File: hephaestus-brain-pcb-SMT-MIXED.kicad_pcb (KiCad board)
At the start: 2 copper layers, 26 x 49 mm, 31 parts, among them IC1 ATSAMD51G19A-MU, J1 Barrel_Jack, J2 Conn_02x03_Odd_Even, J3 USB_B_Micro, J5 Conn_01x03_Male, J6 Conn_01x03_Male, J7 Conn_01x03_Male, SW1 SW_SPDT, SW2 SW_SPST, SW3 SW_SPST, U1 LM1117-5.0, U2 AP2112K-3.3, U3 AT25xxx-MA, U4 74LVC1G125

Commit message: routing tweaks
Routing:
- net +5V: track 33.1 -> 33.7 mm
- net RX: vias 1 -> 2

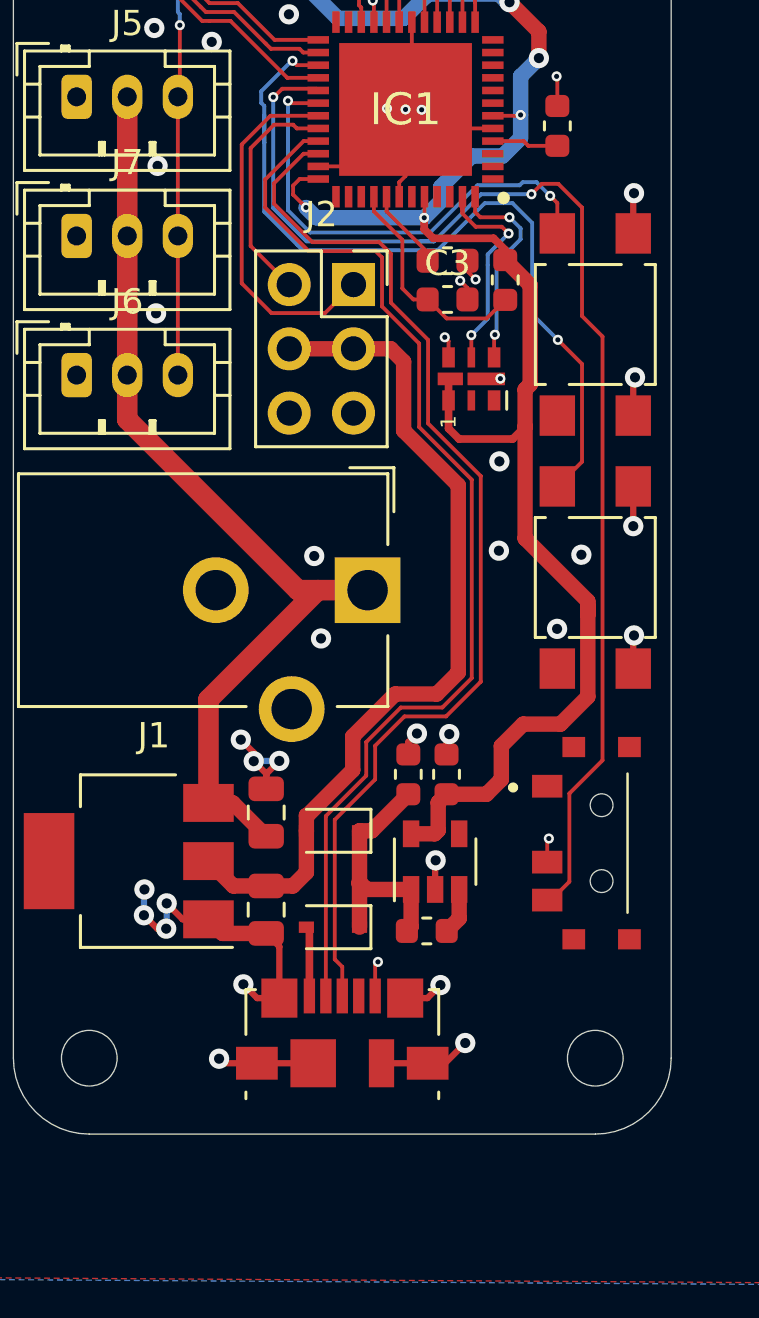
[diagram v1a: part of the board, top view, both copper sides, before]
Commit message: Switched over to USBC connector.
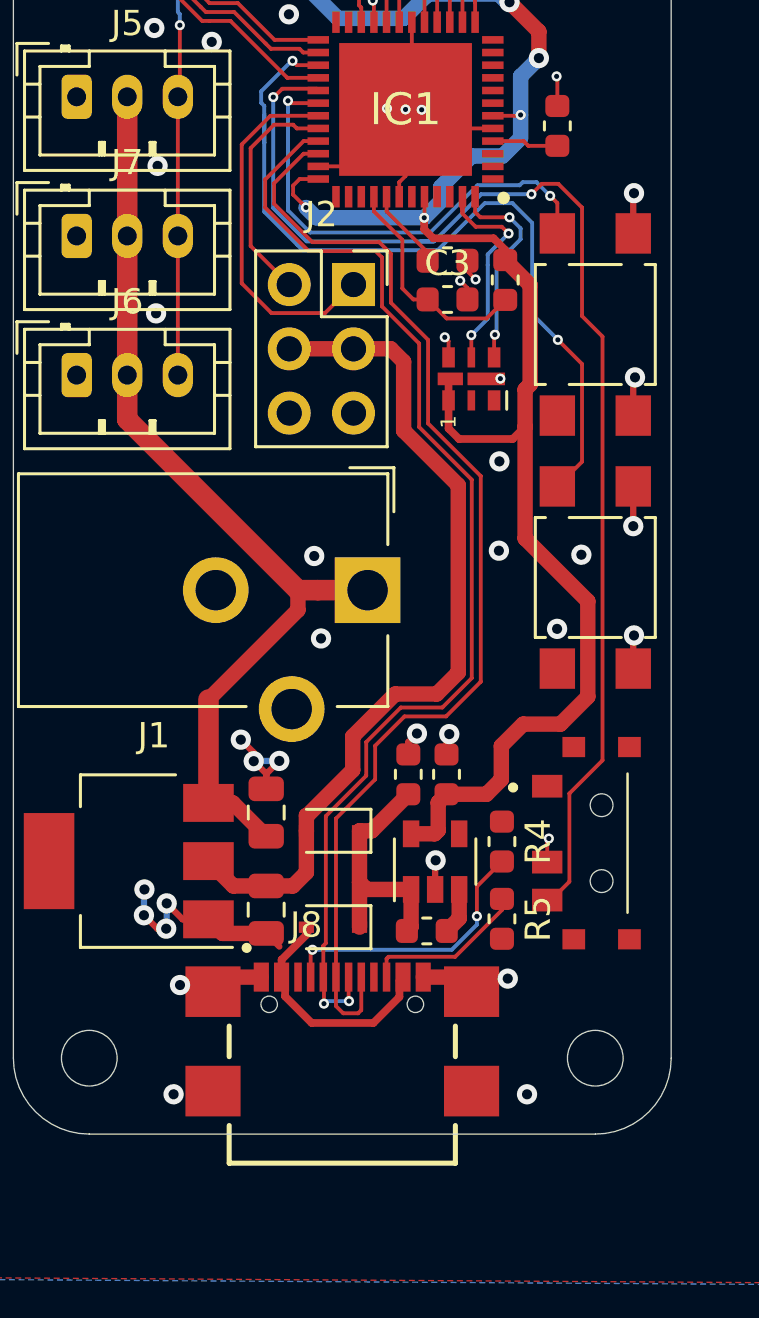
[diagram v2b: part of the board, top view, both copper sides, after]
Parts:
- removed J3: USB_B_Micro, Connector_USB:USB_Micro-B_Molex_47346-0001
- added J8: USB4110-GF-A, unified:GCT_USB4110-GF-A, F.Cu at (123.0, 102.9)
- added R4: 5.1k, Resistor_SMD:R_0603_1608Metric, F.Cu at (129.3, 96.4)
- added R5: 5.1k, Resistor_SMD:R_0603_1608Metric, F.Cu at (129.3, 99.5)
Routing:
- net Net-(J8-PadA5): track 0.00 -> 10.9 mm, vias 0 -> 2
- net GND: track 77.1 -> 67.2 mm, vias 42 -> 41
- net +5VP: track 2.77 -> 9.59 mm
- net Net-(J8-PadB5): track 0.00 -> 6.52 mm
- net D+: track 42.8 -> 45.5 mm
- net D-: track 43.3 -> 45.6 mm, vias 0 -> 2
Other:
- rule pad_to_mask_clearance: 0.051 -> 0.0005

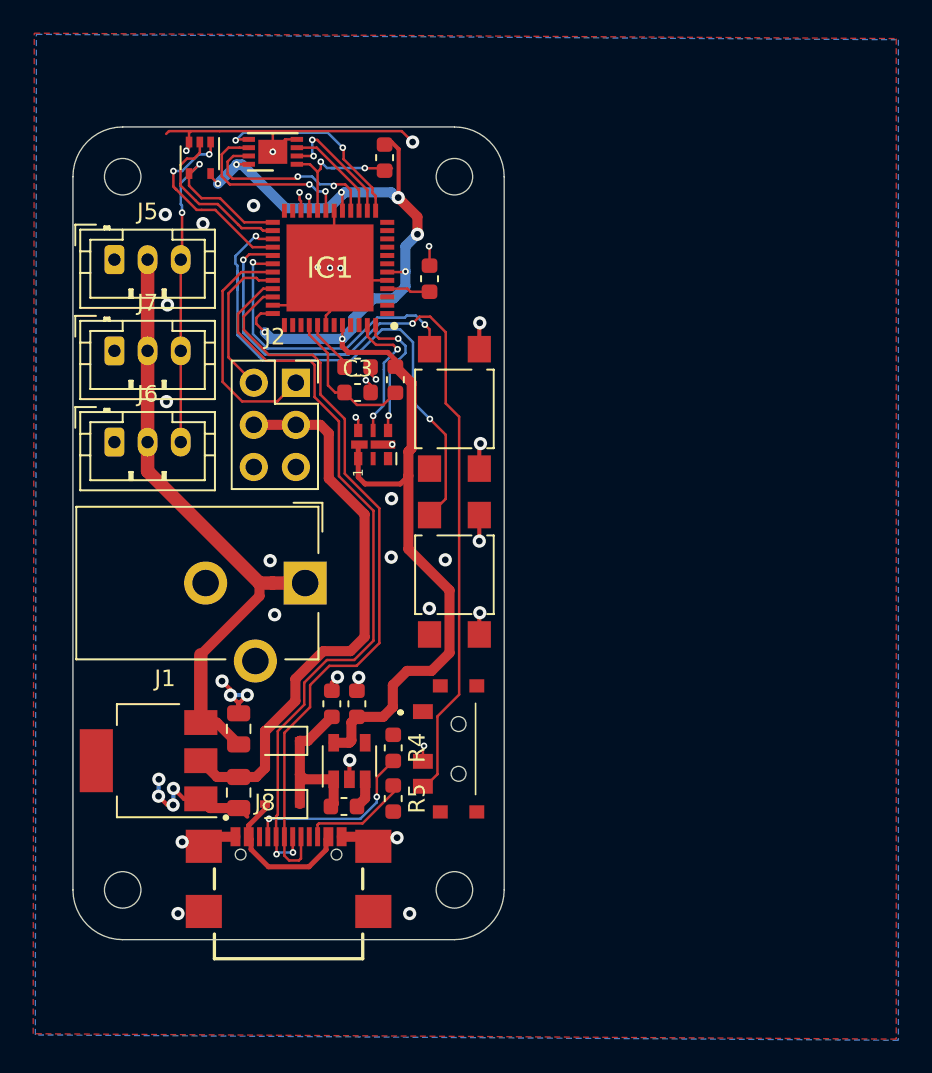
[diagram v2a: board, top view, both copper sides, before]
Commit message: Added SWD Connector and QWIIC
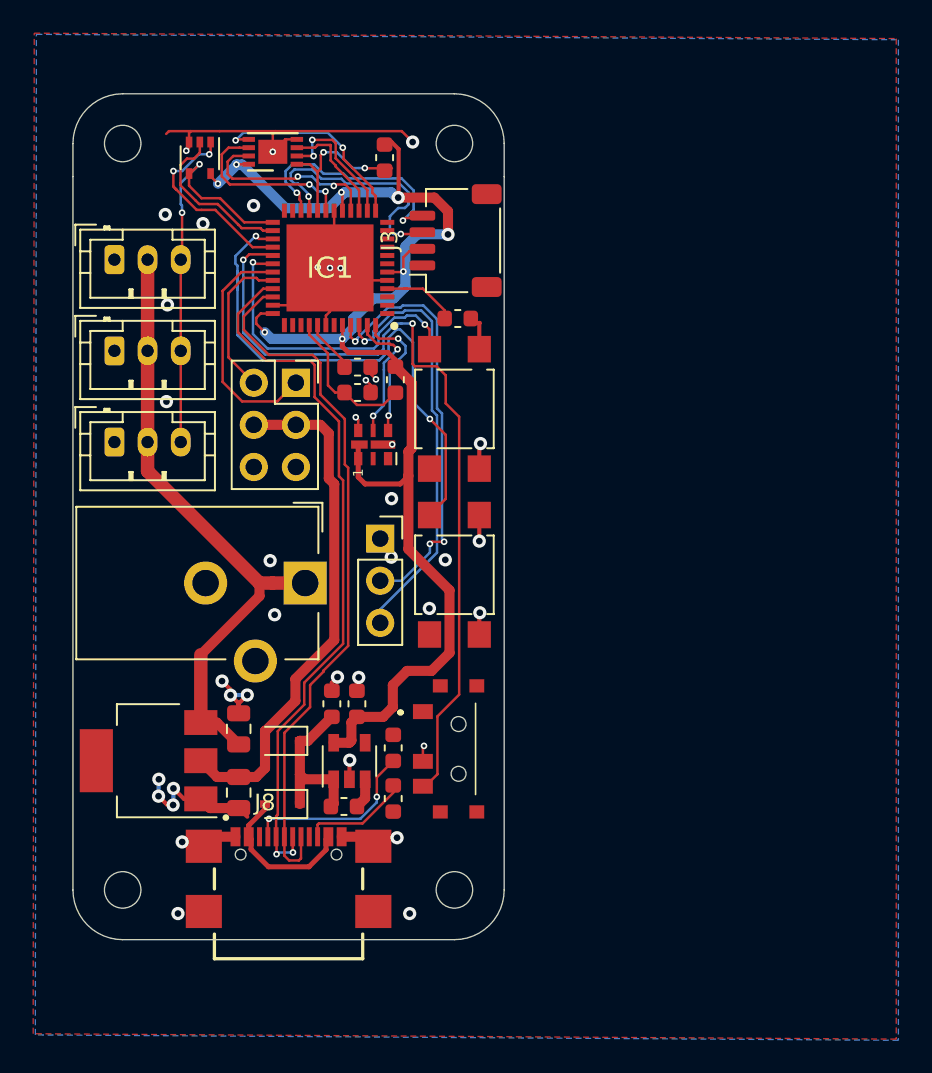
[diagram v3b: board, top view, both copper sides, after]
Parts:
- added J3: StemmaQT, Connector_JST:JST_SH_SM04B-SRSS-TB_1x04-1MP_P1.00mm_Horizontal, F.Cu at (133.1, 65.8)
- added J4: Conn_01x03_Female, Connector_PinSocket_2.54mm:PinSocket_1x03_P2.54mm_Vertical, F.Cu at (128.5, 83.8)
- moved C5 2.94 mm to (133.2, 70.5), turned to 180 degrees
- moved H3 2.00 mm to (113.0, 60.0)
- moved H4 2.00 mm to (133.0, 60.0)
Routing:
- net SWCLK: track 0.00 -> 26.1 mm, vias 0 -> 3
- net SWDIO: track 0.00 -> 26.1 mm, vias 0 -> 1
- net SDA: track 0.87 -> 15.7 mm, vias 1 -> 2
- net SCL: track 1.14 -> 14.6 mm, vias 1 -> 2
- net +3V3: track 79.5 -> 85.6 mm
- net D+: track 45.5 -> 43.0 mm
- net +5V: track 33.7 -> 31.2 mm
- net D-: track 45.6 -> 43.1 mm
- net Net-(C5-Pad2): track 2.63 -> 4.71 mm
- net GND: track 67.2 -> 66.1 mm, vias 41 -> 39
- net QSPI_D2: track 6.06 -> 6.77 mm
- net QSPI_CS: track 9.09 -> 9.64 mm
- net QSPI_D1: track 7.84 -> 8.38 mm
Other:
- board size 26 x 49 mm -> 26 x 51 mm

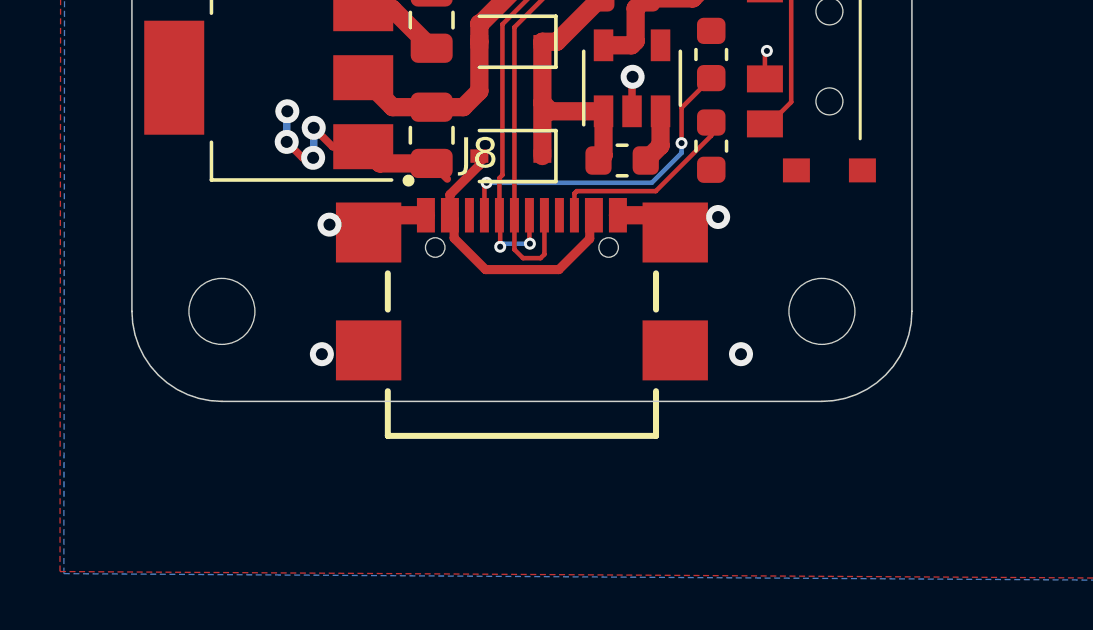
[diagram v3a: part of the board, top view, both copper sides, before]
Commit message: Added more robust USBC Connector
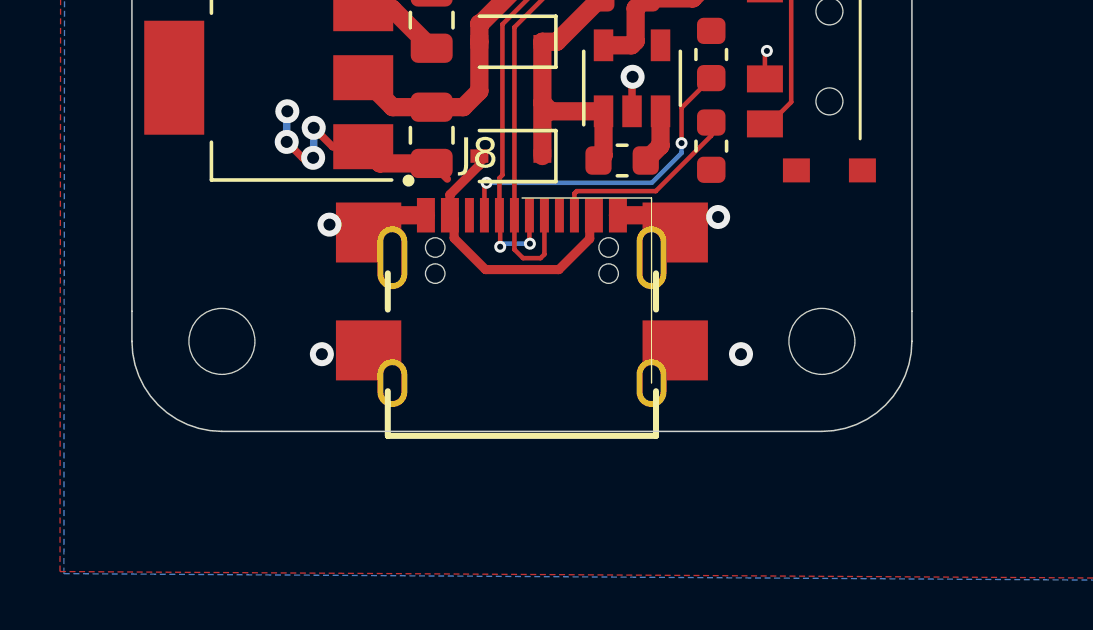
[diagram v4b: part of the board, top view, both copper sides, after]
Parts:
- moved H1 1.00 mm to (113.0, 106.0)
- moved H2 1.00 mm to (133.0, 106.0)
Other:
- board size 26 x 51 mm -> 26 x 52 mm

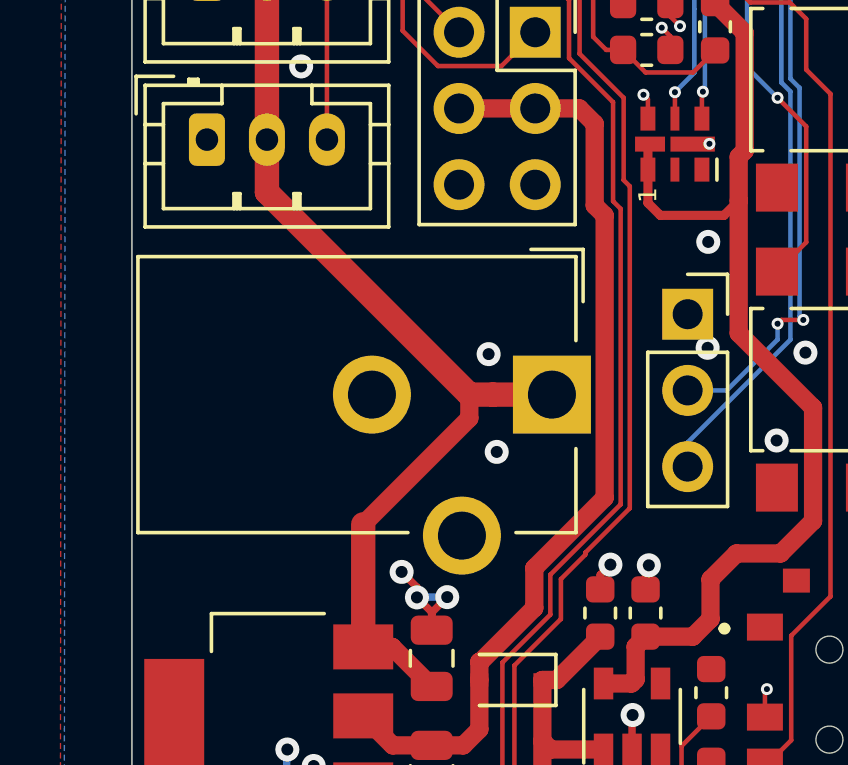
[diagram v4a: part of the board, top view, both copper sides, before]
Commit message: Swapped out barrel jack footprint.
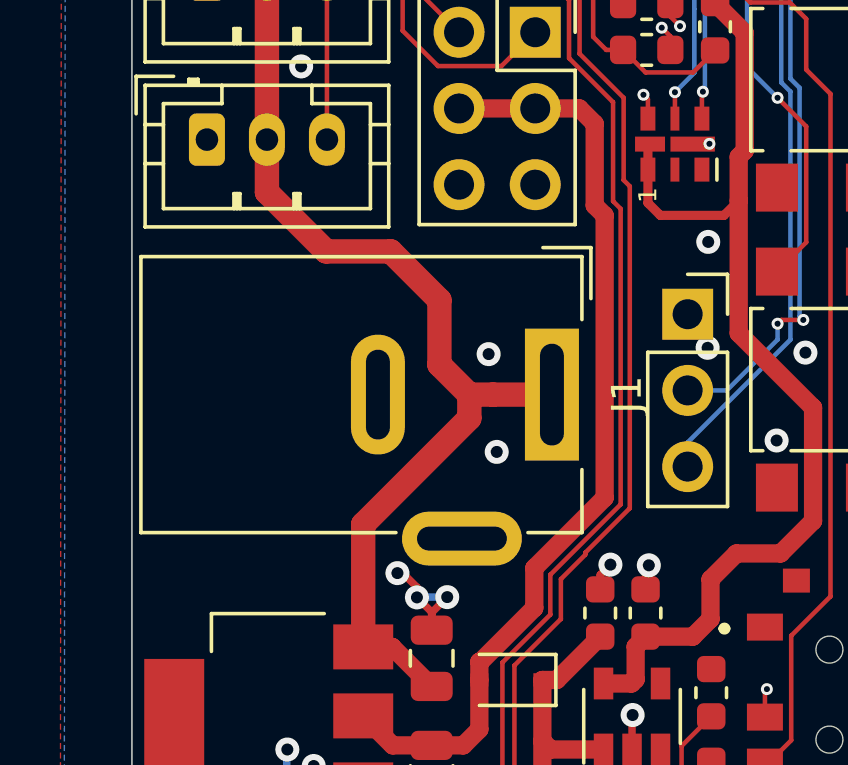
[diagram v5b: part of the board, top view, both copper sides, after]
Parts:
- J1: footprint Connector_BarrelJack:BarrelJack_CUI_PJ-102AH_Horizontal -> Connector_BarrelJack:BarrelJack_Wuerth_6941xx301002
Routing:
- net VCC: track 37.8 -> 39.0 mm

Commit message: Fixed soldermask issue.
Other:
- rule solder_mask_min_width: 0.25 -> 0.0005
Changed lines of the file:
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@@
   (layers
     (0 F.Cu signal)
-    (31 B.Cu signal)
+    (31 B.Cu signal hide)
     (32 B.Adhes user)
     (33 F.Adhes user)
@@
     (pad_drill 0.762)
     (pad_to_mask_clearance 0.0005)
-    (solder_mask_min_width 0.25)
+    (solder_mask_min_width 0.0005)
     (aux_axis_origin 0 0)
     (visible_elements 7FFFFFFF)
     (pcbplotparams
-      (layerselection 0x010fc_ffffffff)
+      (layerselection 0x00080_7ffffffe)
       (usegerberextensions false)
       (usegerberattributes false)
       (usegerberadvancedattributes false)
       (creategerberjobfile false)
-      (excludeedgelayer true)
+      (excludeedgelayer false)
       (linewidth 0.100000)
       (plotframeref false)
@@
       (padsonsilk false)
       (subtractmaskfromsilk false)
-      (outputformat 1)
+      (outputformat 5)
       (mirror false)
       (drillshape 0)

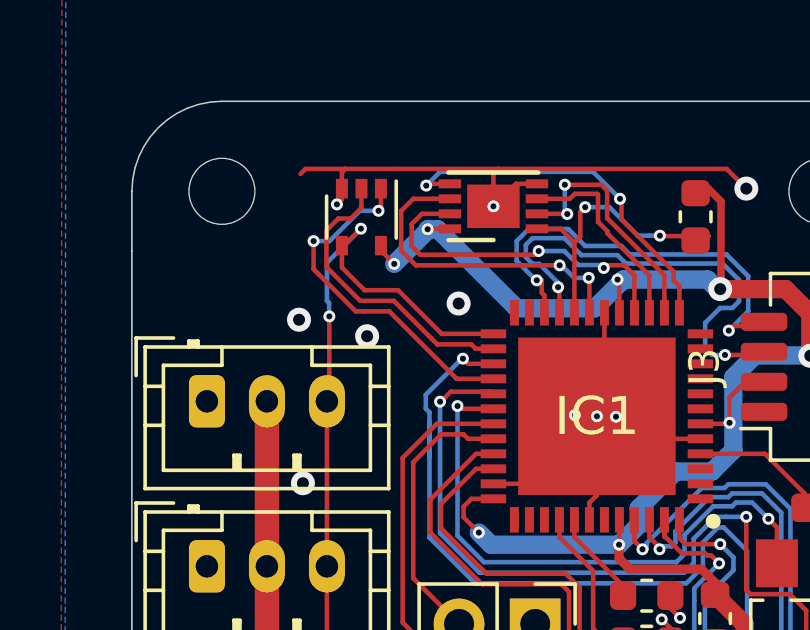
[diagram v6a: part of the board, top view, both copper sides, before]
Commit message: Added board Artwork
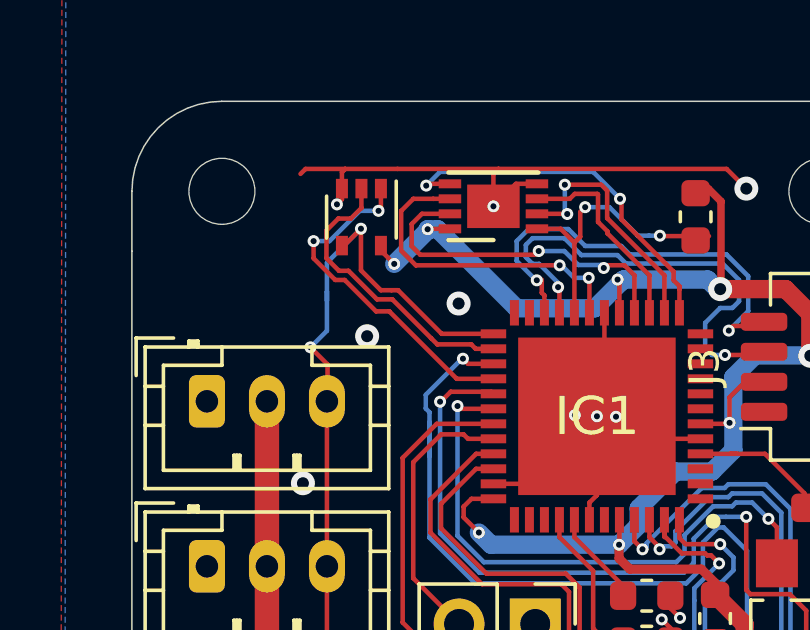
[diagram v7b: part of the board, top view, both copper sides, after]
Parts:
- added Ref**: Val**, unified:PCB-artwork, F.Cu at (123.0, 83.0)
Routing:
- net RX: track 24.8 -> 25.8 mm
- net GND: vias 39 -> 38
